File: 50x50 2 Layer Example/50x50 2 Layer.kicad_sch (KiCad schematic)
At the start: 73 parts, among them J1 Conn_01x02, J2 USB_C_Receptacle_USB2.0_14P, J3 Conn_01x03, J4 Conn_01x04, Q1 MMBT3904, SW1 PWR_SELECT, SW3 Reset, SW4 ON_SW, U1 W25Q32JVSSIQ, U2 USBLC6-2SC6, U3 Voltage Regulator (MCP1755S-3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, U4 RP2354A, U5 Sensor Board, Y1 12MHz

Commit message: Fixed RP2354A Schematic Added LCSC Part Numbers Added Datasheets
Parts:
- removed BZ2: Buzzer, Buzzer_Beeper:Buzzer_Murata_PKMCS0909E, symbol Device:Buzzer
- removed L1: 3.3u, Footprints:IND-SMD_L2.0-W1.6_AOTA-B201610S3R3-101-T, symbol Device:L_Small
- removed Q1: MMBT3904, Package_TO_SOT_SMD:SOT-23, symbol Transistor_BJT:MMBT3904
- removed R16: 1k, Capacitor_SMD:C_0603_1608Metric_Pad1.08x0.95mm_HandSolder, symbol Device:R
- removed U4: RP2354A, Package_DFN_QFN:QFN-60-1EP_7x7mm_P0.4mm_EP3.4x3.4mm, symbol MCU_RaspberryPi:RP2354A
- added BZ3: Buzzer, Buzzer_Beeper:Buzzer_Murata_PKMCS0909E, symbol Device:Buzzer
- added C21, C22, C23: 100n, Capacitor_SMD:C_0603_1608Metric_Pad1.08x0.95mm_HandSolder, symbol Device:C
- added C24: 10u, Capacitor_SMD:C_0805_2012Metric, symbol Device:C
- added L1: 3.3u, Footprints:IND-SMD_L2.0-W1.6_AOTA-B201610S3R3-101-T, symbol Device:L
- added Q2: MMBT3904, Package_TO_SOT_SMD:SOT-23, symbol Transistor_BJT:MMBT3904
- added R26, R27: 1k, Resistor_SMD:R_0603_1608Metric_Pad0.98x0.95mm_HandSolder, symbol Device:R
- added SW2: SW_Push, Button_Switch_SMD:SW_SPST_TS-1088-xR020, symbol Switch:SW_Push
- added U4: RP2354_60QFN, Package_DFN_QFN:QFN-60-1EP_7x7mm_P0.4mm_EP3.4x3.4mm_ThermalVias, symbol MCU_RaspberryPi_RP2350:RP2350_60QFN
- C13: value 4.7u -> 100n
- C14, C15: value 100n -> 4.7u; LCSC Part Number C28233 -> (none); MPN CL21B104KCFNNNE -> (none)
- C16, C17, C18, C19: LCSC Part Number C28233 -> (none); MPN CL21B104KCFNNNE -> (none)
- C20: value 10u -> 100n; footprint Capacitor_SMD:C_0805_2012Metric_Pad1.18x1.45mm_HandSolder -> Capacitor_SMD:C_0603_1608Metric_Pad1.08x0.95mm_HandSolder; LCSC Part Number C28323 -> (none); MPN CL21B105KBFNNNE -> (none)
- C3, C6: footprint Capacitor_SMD:C_0603_1608Metric_Pad1.08x0.95mm_HandSolder -> Capacitor_SMD:C_0805_2012Metric
- D1: value Blue LED -> Yellow LED; footprint LED_SMD:LED_0805_2012Metric_Pad1.15x1.40mm_HandSolder -> LED_SMD:LED_0805_2012Metric
- D10: value LED -> Green LED; footprint LED_SMD:LED_0402_1005Metric_Pad0.77x0.64mm_HandSolder -> LED_SMD:LED_0805_2012Metric
- D4, D5: footprint LED_SMD:LED_0805_2012Metric_Pad1.15x1.40mm_HandSolder -> LED_SMD:LED_0805_2012Metric
- D8: value LED -> Red LED; footprint LED_SMD:LED_0402_1005Metric_Pad0.77x0.64mm_HandSolder -> LED_SMD:LED_0805_2012Metric
- D9: value LED -> Yellow LED; footprint LED_SMD:LED_0402_1005Metric_Pad0.77x0.64mm_HandSolder -> LED_SMD:LED_0805_2012Metric
- R10: footprint Capacitor_SMD:C_0603_1608Metric_Pad1.08x0.95mm_HandSolder -> Resistor_SMD:R_0603_1608Metric_Pad0.98x0.95mm_HandSolder; LCSC Part Number C17414 -> (none); MPN RC0805FR-074K7L -> (none)
- R11: value 360 -> 390
- R12: footprint Capacitor_SMD:C_0603_1608Metric_Pad1.08x0.95mm_HandSolder -> Resistor_SMD:R_0402_1005Metric
- R13: value 27 -> 1k; footprint Capacitor_SMD:C_0603_1608Metric_Pad1.08x0.95mm_HandSolder -> Resistor_SMD:R_0603_1608Metric_Pad0.98x0.95mm_HandSolder; LCSC Part Number C17588 -> (none); MPN 0805W8F274JT5E -> (none)
- R14: footprint Capacitor_SMD:C_0603_1608Metric_Pad1.08x0.95mm_HandSolder -> Resistor_SMD:R_0603_1608Metric_Pad0.98x0.95mm_HandSolder; LCSC Part Number C17588 -> (none); MPN 0805W8F274JT5E -> (none)
- R15: value 1k -> 27; footprint Capacitor_SMD:C_0603_1608Metric_Pad1.08x0.95mm_HandSolder -> Resistor_SMD:R_0603_1608Metric_Pad0.98x0.95mm_HandSolder; MPN RC0805FR-074K7L -> (none)
- R21, R22, R23: value 80 -> 100
- R3, R6, R7, R8: footprint Resistor_SMD:R_0603_1608Metric -> Resistor_SMD:R_0603_1608Metric_Pad0.98x0.95mm_HandSolder
- R9: footprint Capacitor_SMD:C_0603_1608Metric_Pad1.08x0.95mm_HandSolder -> Resistor_SMD:R_0603_1608Metric_Pad0.98x0.95mm_HandSolder
- SW3: value Reset -> SW_Push; footprint Button_Switch_SMD:SW_SPST_PTS645 -> Button_Switch_SMD:SW_SPST_TS-1088-xR020; LCSC Part Number C2837531 -> (none); MPN KH-6X6X5H-STM -> (none)
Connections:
- net +1V1: now also C12.1, C13.1, C15.1, C16.1, L1.1, U4.23 (DVDD), U4.39 (DVDD), U4.50 (VREG_FB), U4.6 (DVDD); no longer C12.2
- net +3V3: now also C11.1, C20.1, BZ3.1 (+), C21.1, C22.1, C23.1, C24.1, R27.1, U4.1 (IOVDD), U4.11 (IOVDD), U4.20 (IOVDD), U4.30 (IOVDD), U4.38 (IOVDD), U4.44 (ADC_AVDD), U4.45 (IOVDD), U4.49 (VREG_VIN), U4.53 (USB_OTP_VDD), U4.54 (QSPI_IOVDD); no longer C11.2, C14.1, C15.1, C16.1, C20.2
- net ADC_0: now also U4.40 (GPIO26_ADC0)
- net ADC_1: now also U4.41 (GPIO27_ADC1)
- net ADC_2: now also U4.42 (GPIO28_ADC2)
- net ADC_3: now also U4.43 (GPIO29_ADC3)
- net BUZZER: now also R26.2, U4.4 (GPIO2); no longer R15.2
- net CLK_GPIN0: now also U4.32 (GPIO20)
- net CLK_GPOUT0: now also U4.33 (GPIO21)
- net D+: no longer R14.1
- net D-: no longer R13.1
- net GND: now also C11.2, C12.2, C13.2, C20.2, C21.2, C22.2, C23.2, C24.2, Q2.2 (E), SW2.1, U4.47 (VREG_PGND), U4.61 (GND); no longer C11.1, C12.1, C13.1, C20.1
- net GPIO_3: now also U4.5 (GPIO3)
- net GPIO_4: now also U4.7 (GPIO4)
- net GPIO_5: now also U4.8 (GPIO5)
- net GPIO_6: now also U4.9 (GPIO6)
- net GPIO_7: now also U4.10 (GPIO7)
- net I2C0_SCL: now also U4.37 (GPIO25)
- net I2C0_SDA: now also U4.36 (GPIO24)
- net I2C1_SCL: now also U4.35 (GPIO23)
- net I2C1_SDA: now also U4.34 (GPIO22)
- net INT_1: now also U4.12 (GPIO8)
- net LED_GREEN: now also U4.15 (GPIO11)
- net LED_RED: now also U4.13 (GPIO9)
- net LED_RGB: now also U4.3 (GPIO1)
- net LED_YELLOW: now also U4.14 (GPIO10)
- net RUN: now also U4.26 (RUN)
- net SPI0_CSn: now also U4.28 (GPIO17)
- net SPI0_MISO: now also U4.27 (GPIO16)
- net SPI0_MOSI: now also U4.31 (GPIO19)
- net SPI0_SCK: now also U4.29 (GPIO18)
- net SPI1_CSn: now also U4.17 (GPIO13)
- net SPI1_MISO: now also U4.16 (GPIO12)
- net SPI1_MOSI: now also U4.19 (GPIO15)
- net SPI1_SCK: now also U4.18 (GPIO14)
- net SWCLK: now also U4.24 (SWCLK)
- net SWD: now also U4.25 (SWD)
- net USB_D+: now also R14.1; no longer R14.2
- net USB_D-: now also R15.1; no longer R13.2
- net USB_DET: now also U4.2 (GPIO0)
- net XIN: now also U4.21 (XIN)
- net XOUT: now also U4.22 (XOUT)
- net VREG_AVDD: now reaches R12.2
- net VREG_AVDD: now also C14.1, U4.46 (VREG_AVDD); no longer C13.2
- new net: BZ3.2 (-), Q2.3 (C), R27.2
- new net: R15.2, U4.51 (USB_DM)
- new net: R14.2, U4.52 (USB_DP)
- new net: Q2.1 (B), R26.1
- new net QSPI_SS: R13.1, U4.60 (QSPI_SS)
- new net VREG_LX: L1.2, U4.48 (VREG_LX)
- new net ~{USB_BOOT}: R13.2, SW2.2
- no-connect marks 10 -> 9
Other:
- note added: "Make sure R7 and R8 are close to RP2350"
- note added: "Raspberry Pi Microcontroller RP2354A"
- note removed: "Bypass and decoupling capacitors"
- note removed: "RP2354A"
- note removed: "Reset Button"
- moved on the sheet: C1, C10, C2, C3, C4, C5, C6, C7, C8, C9, D1, D2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

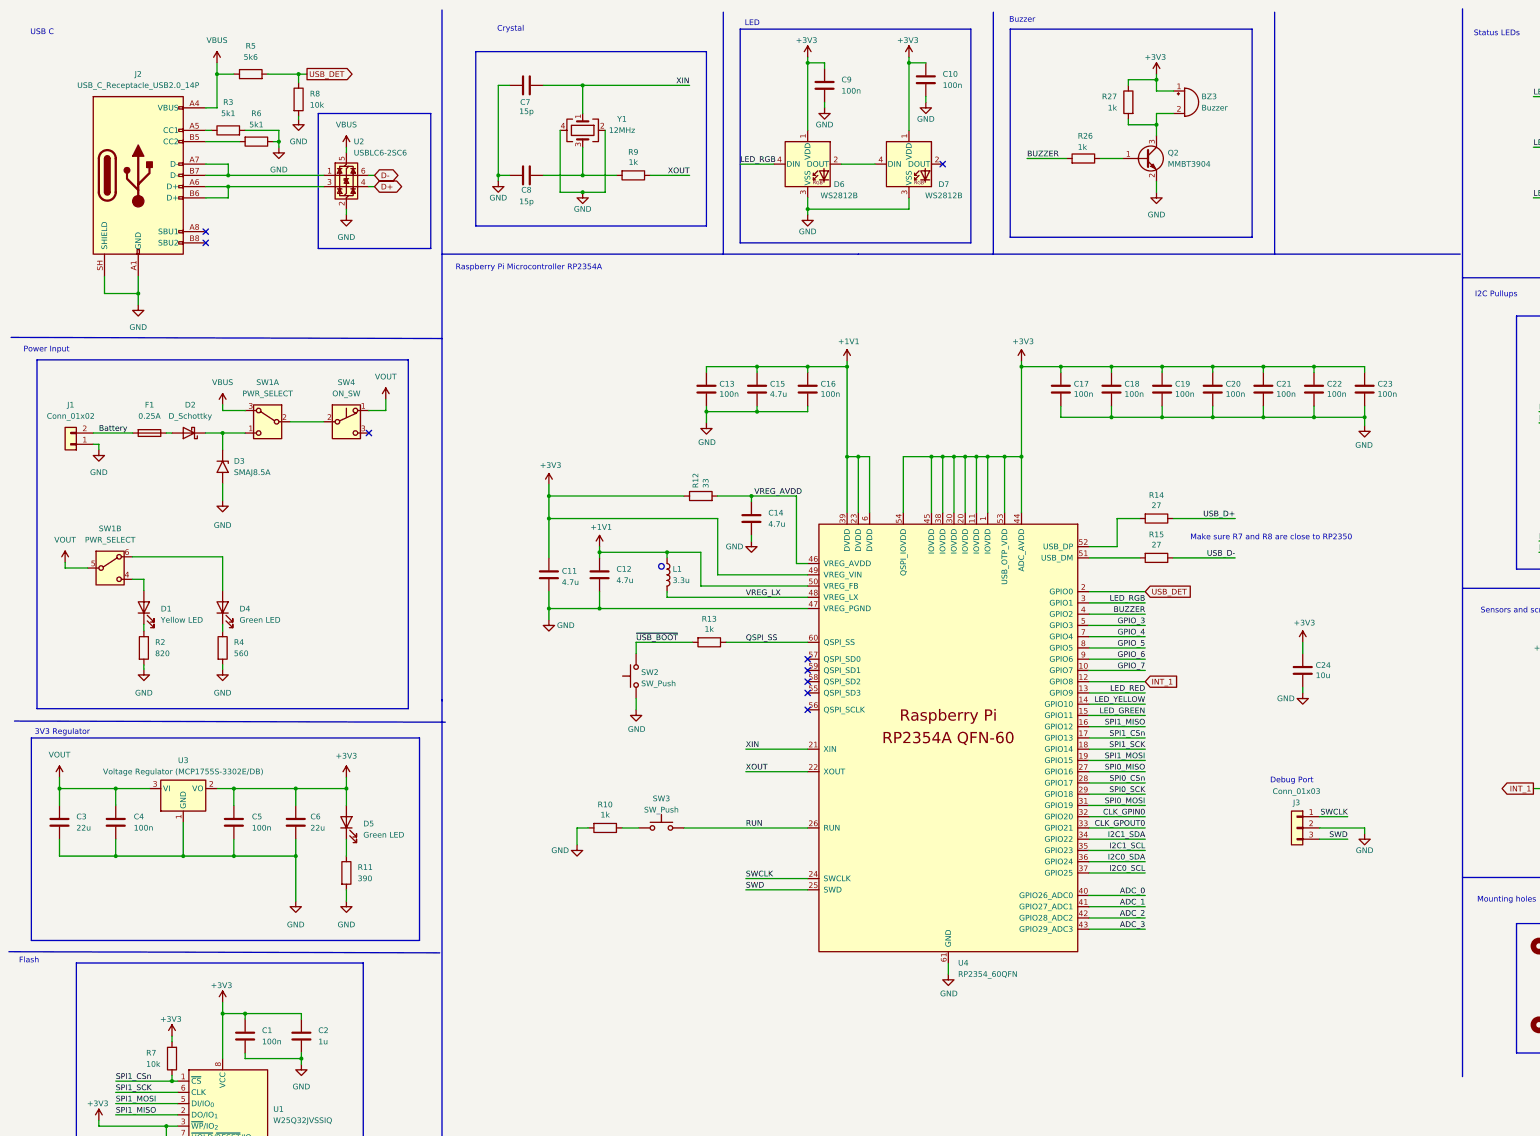
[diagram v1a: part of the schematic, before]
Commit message: Minor changes to Schematic
Adjusted some of the labels, specifically for D- and D+ connected to the USB C
Moved Debug Port and Reset Button back to their own sections
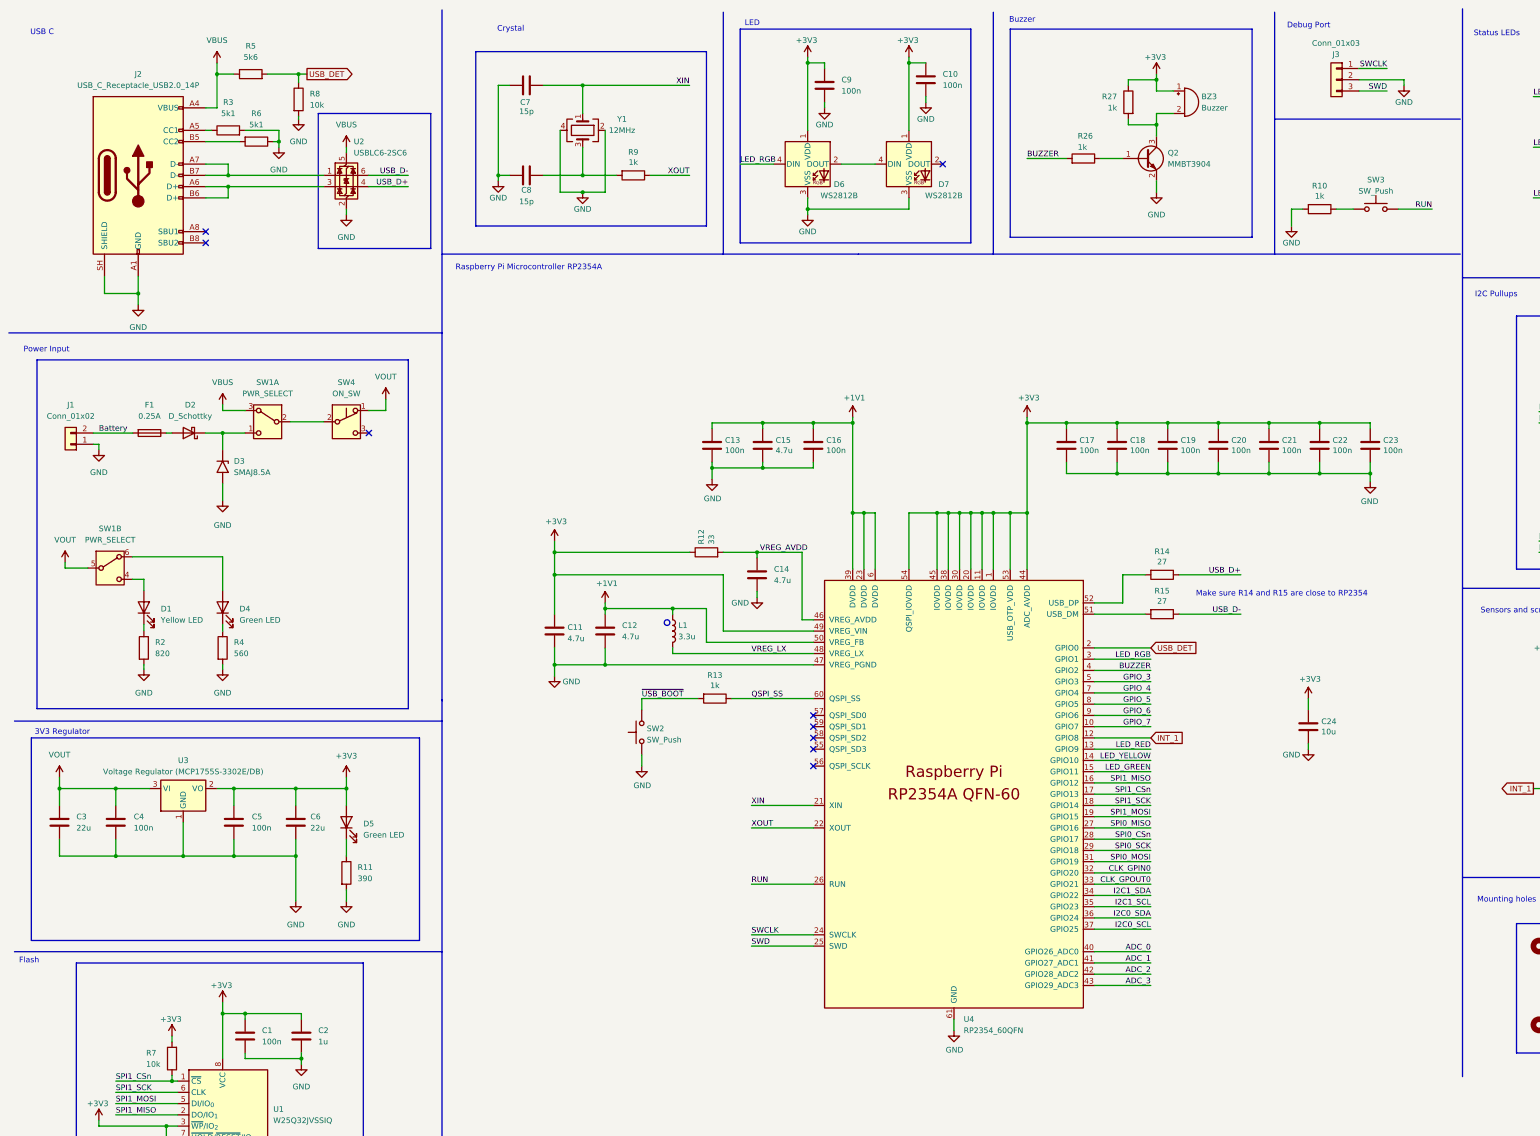
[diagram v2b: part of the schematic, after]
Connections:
- net D+ is gone; now on net USB_D+: U2.4 (I/O2)
- net D- is gone; now on net USB_D-: U2.6 (I/O1)
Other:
- note added: "Make sure R14 and R15 are close to RP2354"
- note removed: "Make sure R7 and R8 are close to RP2350"
- moved on the sheet: C11, C12, C13, C14, C15, C16, C17, C18, C19, C20, C21, C22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
